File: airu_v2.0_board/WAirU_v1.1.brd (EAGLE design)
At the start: 40.3 x 50 mm, 66 parts, among them J2 2p-2.0, Q2 MMBT3904LT1G, Q3 MMBT3904LT1G, Q4 BSS84, Q6 BSS84, U1 MOLEX-53261-0871, U2 CN3065-DFN8, U3 HDC1080DMBT, U4 CJT1117-3.3-SOT223, U5 CH340T-SSOP20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

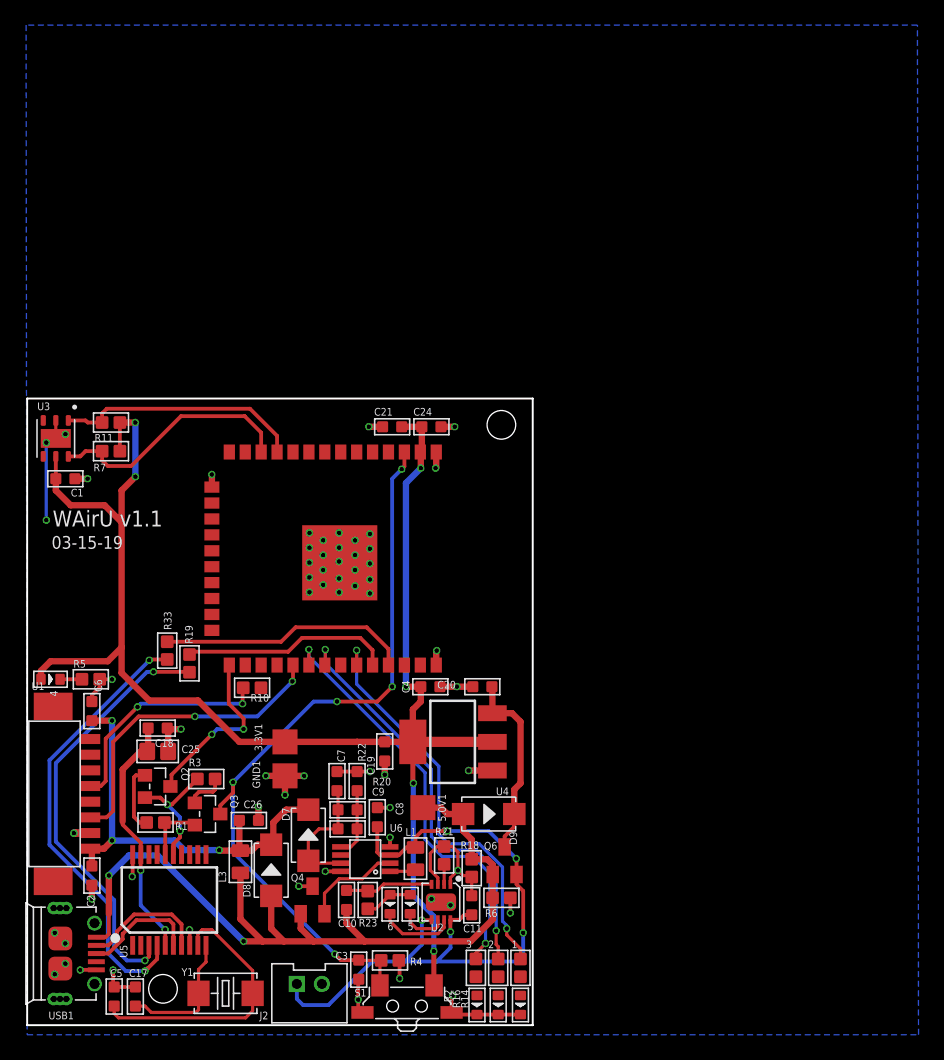
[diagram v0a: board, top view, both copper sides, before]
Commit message: added keepout on temperature sensor
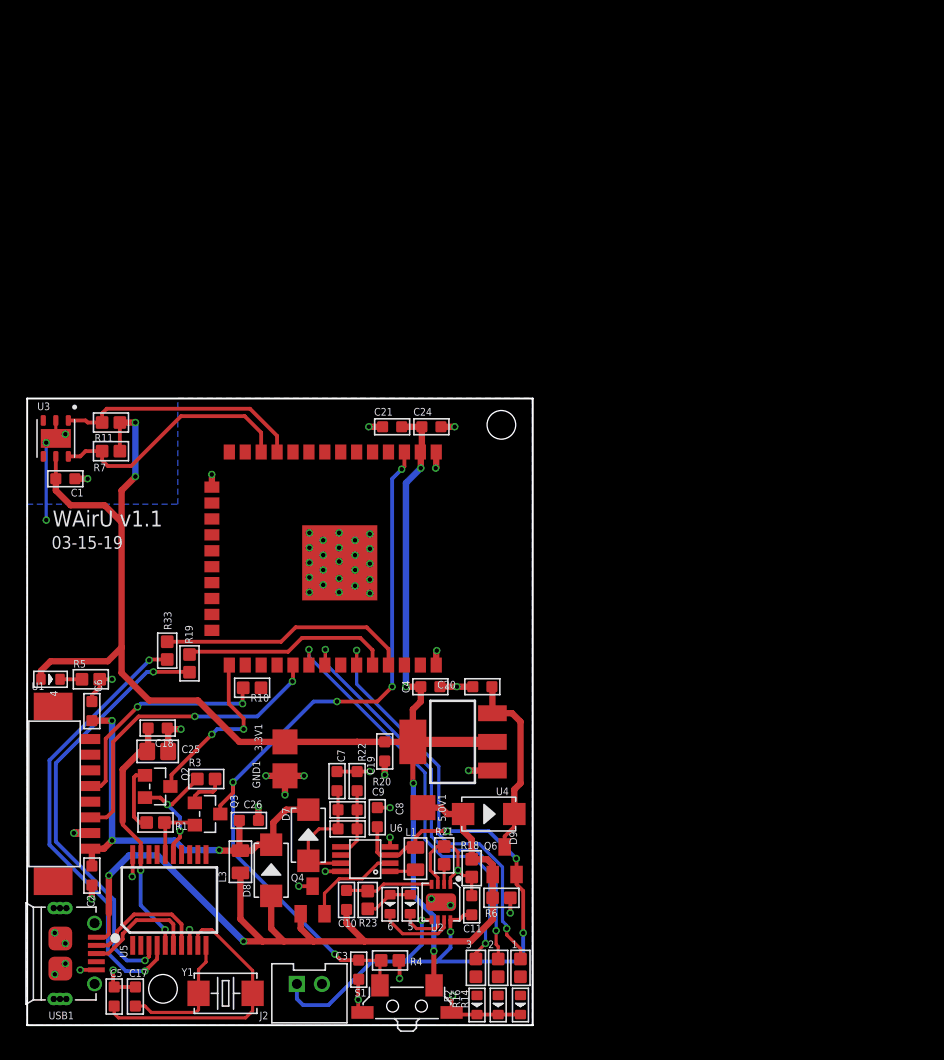
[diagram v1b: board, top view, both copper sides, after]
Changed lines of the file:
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@@
 <text x="1.9471375" y="38.01153125" size="1.016" layer="21" font="vector">03-15-19</text>
 <wire x1="7.9375" y1="-12.7" x2="7.9375" y2="63.5" width="0.254" layer="48" style="longdash"/>
-<rectangle x1="0" y1="41.22854375" x2="12.19078125" y2="50.032996875" layer="39"/>
-<rectangle x1="0" y1="41.22854375" x2="12.19078125" y2="50.032996875" layer="40"/>
-<rectangle x1="0" y1="41.22854375" x2="12.19078125" y2="50.03299375" layer="40"/>
-<rectangle x1="0" y1="41.22854375" x2="12.19078125" y2="50.032996875" layer="41"/>
-<rectangle x1="0" y1="41.22854375" x2="12.19078125" y2="50.032996875" layer="42"/>
 </plain>
 <attributes>
@@
 <contactref element="1" pad="-"/>
 <contactref element="3" pad="-"/>
-<polygon width="0.2032" layer="16">
-<vertex x="0" y="-0.761925"/>
-<vertex x="71.12" y="-0.761925"/>
-<vertex x="71.03534375" y="79.798290625"/>
-<vertex x="-0.08465625" y="79.798290625"/>
-</polygon>
 <contactref element="C19" pad="1"/>
 <contactref element="C20" pad="1"/>
@@
 <wire x1="1.523846875" y1="46.477353125" x2="1.523846875" y2="40.297303125" width="0.254" layer="16"/>
 <via x="1.523846875" y="40.297303125" extent="1-16" drill="0.35"/>
+<polygon width="0.254" layer="16">
+<vertex x="0" y="0"/>
+<vertex x="0" y="41.567175"/>
+<vertex x="12.021465625" y="41.567175"/>
+<vertex x="12.021465625" y="50.032996875"/>
+<vertex x="40.297303125" y="50.032996875"/>
+<vertex x="40.297303125" y="0"/>
+</polygon>
 <wire x1="24.889509375" y1="36.995634375" x2="24.939640625" y2="36.891425" width="0" layer="19" extent="1-1"/>
 <wire x1="2.2857625" y1="46.815984375" x2="2.370428125" y2="46.477353125" width="0" layer="19" extent="1-16"/>
+<wire x1="3.80969375" y1="43.598978125" x2="2.370428125" y2="46.477353125" width="0" layer="19" extent="1-16"/>
 </signal>
 <signal name="3.3V">
